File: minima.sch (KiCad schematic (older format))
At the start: 13 parts, among them J101 left_output, J102 left_input, J103 right_output, J104 right_input, J105 aux_power, J106 mains_voltage, J107 transformer_secondary, J108 transformer_primary, J109 earth

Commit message: The board shall now support single channel only.
Signed-off-by: Nenad Radulovic <nenad.radulovic@seavus.com>
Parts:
- removed J102: left_input, Connector_PinHeader_2.54mm:PinHeader_1x04_P2.54mm_Vertical, symbol Conn_01x04
- removed J103: right_output, Connector_Phoenix_MC:PhoenixContact_MCV_1,5_2-G-3.5_1x02_P3.50mm_Vertical, symbol Screw_Terminal_01x02
- removed J104: right_input, Connector_PinHeader_2.54mm:PinHeader_1x04_P2.54mm_Vertical, symbol Conn_01x04
- removed J105: aux_power, Connector_Phoenix_MC:PhoenixContact_MCV_1,5_4-G-3.5_1x04_P3.50mm_Vertical, symbol Conn_01x04
- removed J106: mains_voltage, Connector_Phoenix_MC:PhoenixContact_MCV_1,5_2-G-3.81_1x02_P3.81mm_Vertical, symbol Screw_Terminal_01x02
- removed J107: transformer_secondary, Connector_Phoenix_MC:PhoenixContact_MCV_1,5_3-G-3.5_1x03_P3.50mm_Vertical, symbol Screw_Terminal_01x03
- removed J108: transformer_primary, Connector_Phoenix_MC:PhoenixContact_MCV_1,5_2-G-3.81_1x02_P3.81mm_Vertical, symbol Screw_Terminal_01x02
- removed J109: earth, Connector_Phoenix_MC:PhoenixContact_MCV_1,5_2-G-5.08_1x02_P5.08mm_Vertical, symbol Screw_Terminal_01x02
- removed MH1, MH2: Mounting hole, MountingHole:MountingHole_3.2mm_M3_ISO14580_Pad, symbol Conn_01x01
- removed MH3, MH4: Mounting Hole, MountingHole:MountingHole_3.2mm_M3_ISO14580_Pad, symbol Conn_01x01
- added J102: input, TerminalBlock_Phoenix:TerminalBlock_Phoenix_MPT-0,5-4-2.54_1x04_P2.54mm_Horizontal, symbol Screw_Terminal_01x04
- added J103: powersupply, Connector_Phoenix_MC:PhoenixContact_MCV_1,5_6-G-3.5_1x06_P3.50mm_Vertical, symbol Screw_Terminal_01x06
- added J104: ps_ctrl, Connector_IDC:IDC-Header_2x05_P2.54mm_Vertical, symbol Conn_02x05_Odd_Even
- added LOGO1: KiCad Logo, Symbol:KiCad-Logo2_12mm_SilkScreen, symbol Mounting_Hole
- added LOGO2: OSHW Logo, Symbol:OSHW-Logo2_14.6x12mm_SilkScreen, symbol Mounting_Hole
- added MK101, MK102, MK103, MK104: Mounting_Hole, MountingHole:MountingHole_3.2mm_M3_ISO7380, symbol Mounting_Hole
- J101: value left_output -> output
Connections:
- net labels removed: GNDPWR, VDDA, VSSA
- wire segments 47 -> 57
- no-connect marks 4 -> 1
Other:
- note added: "ps_ctrl_gnd"
- note added: "ps_ctrl_i_reserved"
- note added: "ps_ctrl_o_reserved"
- note added: "ps_ctrl_op"
- note added: "ps_ctrl_outp"
- note added: "ps_ctrl_ovrld"
- note added: "ps_ctrl_vdd12"
- moved on the sheet: J101

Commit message: Switched to Kicad 5.0
Signed-off-by: Nenad Radulovic <nenad.b.radulovic@gmail.com>
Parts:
- removed J104: ps_ctrl, Connector_IDC:IDC-Header_2x05_P2.54mm_Vertical, symbol Conn_02x05_Odd_Even
- J1: renamed from J101; symbol Screw_Terminal_01x02 -> minima-rescue:Screw_Terminal_01x02
- J2: renamed from J102; symbol Screw_Terminal_01x04 -> minima-rescue:Screw_Terminal_01x04
- J3: renamed from J103; footprint Connector_Phoenix_MC:PhoenixContact_MCV_1,5_6-G-3.5_1x06_P3.50mm_Vertical -> Connector_Phoenix_MC:PhoenixContact_MCV_1,5_3-G-3.5_1x03_P3.50mm_Vertical; symbol Screw_Terminal_01x06 -> minima-rescue:Screw_Terminal_01x03
- LOGO1, LOGO2: symbol Mounting_Hole -> minima-rescue:Mounting_Hole
- MK1: renamed from MK101; symbol Mounting_Hole -> minima-rescue:Mounting_Hole
- MK2: renamed from MK102; symbol Mounting_Hole -> minima-rescue:Mounting_Hole
- MK3: renamed from MK103; symbol Mounting_Hole -> minima-rescue:Mounting_Hole
- MK4: renamed from MK104; symbol Mounting_Hole -> minima-rescue:Mounting_Hole
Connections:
- net labels added: GNDPWR
- wire segments 57 -> 18
- no-connect marks 1 -> 0
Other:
- note removed: "ps_ctrl_gnd"
- note removed: "ps_ctrl_i_reserved"
- note removed: "ps_ctrl_o_reserved"
- note removed: "ps_ctrl_op"
- note removed: "ps_ctrl_outp"
- note removed: "ps_ctrl_ovrld"
- note removed: "ps_ctrl_vdd12"
- moved on the sheet: J2

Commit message: Updated regarding v5.0
Still updateing regarding transition to v5.0
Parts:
- removed LOGO1: KiCad Logo, Symbol:KiCad-Logo2_12mm_SilkScreen, symbol minima-rescue:Mounting_Hole
- J1: symbol minima-rescue:Screw_Terminal_01x02 -> Connector:Screw_Terminal_01x02
- J2: symbol minima-rescue:Screw_Terminal_01x04 -> Connector:Screw_Terminal_01x04
- J3: symbol minima-rescue:Screw_Terminal_01x03 -> Connector:Screw_Terminal_01x03
- LOGO2: symbol minima-rescue:Mounting_Hole -> Graphic:Logo_Open_Hardware_Small
- MK1, MK2, MK3, MK4: symbol minima-rescue:Mounting_Hole -> Mechanical:MountingHole
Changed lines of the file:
@@
 $EndSheet
 $Comp
-L minima-rescue:Screw_Terminal_01x02 J1
+L Connector:Screw_Terminal_01x02 J1
 U 1 1 5ABB2BD1
 P 9100 1800
@@
 Connection ~ 2800 2100
 $Comp
-L minima-rescue:Mounting_Hole MK1
+L Mechanical:MountingHole MK1
 U 1 1 5AE4F4CA
 P 1200 6900
@@
 $EndComp
 $Comp
-L minima-rescue:Mounting_Hole MK3
+L Mechanical:MountingHole MK3
 U 1 1 5AE4FF11
 P 1200 7200
@@
 $EndComp
 $Comp
-L minima-rescue:Mounting_Hole MK4
+L Mechanical:MountingHole MK4
 U 1 1 5AE4FFFC
 P 2200 7200
@@
 $EndComp
 $Comp
-L minima-rescue:Mounting_Hole MK2
+L Mechanical:MountingHole MK2
 U 1 1 5AE500F0
 P 2200 6900
@@
 $EndComp
 $Comp
-L minima-rescue:Screw_Terminal_01x04 J2
+L Connector:Screw_Terminal_01x04 J2
 U 1 1 5AE50566
 P 2500 1900
@@
 $EndComp
 $Comp
-L minima-rescue:Screw_Terminal_01x03 J3
+L Connector:Screw_Terminal_01x03 J3
 U 1 1 5AE51422
 P 5550 4300
@@
 	5750 4200 6400 4200
 $Comp
-L minima-rescue:Mounting_Hole LOGO1
-U 1 1 5AE5636C
-P 2950 6900
-F 0 "LOGO1" H 2950 7100 50  0000 C CNN
-F 1 "KiCad Logo" H 2950 7025 50  0000 C CNN
-F 2 "Symbol:KiCad-Logo2_12mm_SilkScreen" H 2950 6900 50  0001 C CNN
-F 3 "" H 2950 6900 50  0001 C CNN
-	1    2950 6900
-	1    0    0    -1
-$EndComp
-$Comp
-L minima-rescue:Mounting_Hole LOGO2
+L Graphic:Logo_Open_Hardware_Small LOGO2
 U 1 1 5AE56655
 P 2950 7200

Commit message: Version 1.0b
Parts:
- added LOGO2: Kicad_Logo, Symbol:KiCad-Logo_5mm_Copper, symbol Graphic:Logo_Open_Hardware_Small
- J1: renamed from J2; footprint TerminalBlock_Phoenix:TerminalBlock_Phoenix_MPT-0,5-4-2.54_1x04_P2.54mm_Horizontal -> TerminalBlock_Phoenix:TerminalBlock_Phoenix_PT-1,5-3-3.5-H_1x03_P3.50mm_Horizontal; symbol Connector:Screw_Terminal_01x04 -> Connector_Generic:Conn_01x03
- J2: renamed from J3; footprint Connector_Phoenix_MC:PhoenixContact_MCV_1,5_3-G-3.5_1x03_P3.50mm_Vertical -> TerminalBlock_Phoenix:TerminalBlock_Phoenix_MKDS-3-3-5.08_1x03_P5.08mm_Horizontal
- J3: renamed from J1; footprint Connector_Phoenix_MC:PhoenixContact_MCV_1,5_2-G-3.5_1x02_P3.50mm_Vertical -> TerminalBlock_Phoenix:TerminalBlock_Phoenix_MKDS-3-2-5.08_1x02_P5.08mm_Horizontal
- LOGO1: renamed from LOGO2; footprint Symbol:OSHW-Logo2_14.6x12mm_SilkScreen -> Symbol:OSHW-Logo2_7.3x6mm_SilkScreen
- MK1, MK4: footprint MountingHole:MountingHole_3.2mm_M3_ISO7380 -> MountingHole:MountingHole_3.2mm_M3_ISO7380_Pad
- MK2: renamed from MK3; footprint MountingHole:MountingHole_3.2mm_M3_ISO7380 -> MountingHole:MountingHole_3.2mm_M3_ISO7380_Pad
- MK3: renamed from MK2; footprint MountingHole:MountingHole_3.2mm_M3_ISO7380 -> MountingHole:MountingHole_3.2mm_M3_ISO7380_Pad
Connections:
- wire segments 18 -> 16
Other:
- moved on the sheet: J3
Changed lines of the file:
@@
 F0 "Power supply" 60
 F1 "psupply.sch" 60
-F2 "ps_vcc" I L 6400 4200 60
-F3 "ps_vee" I L 6400 4300 60
-F4 "ps_gnd" I L 6400 4400 60
+F2 "ps_vcc" I L 6400 4400 60
+F3 "ps_vee" I L 6400 4200 60
+F4 "ps_gnd" I L 6400 4300 60
 $EndSheet
 $Comp
-L Connector:Screw_Terminal_01x02 J1
+L Connector:Screw_Terminal_01x02 J3
 U 1 1 5ABB2BD1
-P 9100 1800
-F 0 "J1" H 9100 1900 50  0000 C CNN
-F 1 "output" H 9100 1600 50  0000 C CNN
-F 2 "Connector_Phoenix_MC:PhoenixContact_MCV_1,5_2-G-3.5_1x02_P3.50mm_Vertical" H 9100 1800 50  0001 C CNN
-F 3 "http://www.farnell.com/datasheets/2138280.pdf" H 9100 1800 50  0001 C CNN
-F 4 "Farnell:3704816" H 9100 1800 60  0001 C CNN "Vendor"
-F 5 "Phoenix:1843606" H 9100 1800 60  0001 C CNN "Manufacturer"
-	1    9100 1800
+P 9100 1700
+F 0 "J3" H 9100 1800 50  0000 C CNN
+F 1 "output" H 9100 1500 50  0000 C CNN
+F 2 "TerminalBlock_Phoenix:TerminalBlock_Phoenix_MKDS-3-2-5.08_1x02_P5.08mm_Horizontal" H 9100 1700 50  0001 C CNN
+F 3 "http://www.farnell.com/datasheets/2138280.pdf" H 9100 1700 50  0001 C CNN
+F 4 "Farnell:3704816" H 9100 1700 60  0001 C CNN "Vendor"
+F 5 "Phoenix:1843606" H 9100 1700 60  0001 C CNN "Manufacturer"
+	1    9100 1700
 	1    0    0    -1
 $EndComp
@@
 Wire Wire Line
 	8000 1800 8900 1800
-Wire Wire Line
-	2700 2100 2800 2100
 Wire Notes Line
 	800  6600 2600 6600
@@
 Text Notes 800  6550 0    60   ~ 0
 Mounting components
-Connection ~ 2800 2100
 $Comp
 L Mechanical:MountingHole MK1
@@
 F 0 "MK1" H 1200 7100 50  0000 C CNN
 F 1 "Mounting_Hole" H 1200 7025 50  0000 C CNN
-F 2 "MountingHole:MountingHole_3.2mm_M3_ISO7380" H 1200 6900 50  0001 C CNN
+F 2 "MountingHole:MountingHole_3.2mm_M3_ISO7380_Pad" H 1200 6900 50  0001 C CNN
 F 3 "" H 1200 6900 50  0001 C CNN
 	1    1200 6900
@@
 $EndComp
 $Comp
-L Mechanical:MountingHole MK3
+L Mechanical:MountingHole MK2
 U 1 1 5AE4FF11
 P 1200 7200
-F 0 "MK3" H 1200 7400 50  0000 C CNN
+F 0 "MK2" H 1200 7400 50  0000 C CNN
 F 1 "Mounting_Hole" H 1200 7325 50  0000 C CNN
-F 2 "MountingHole:MountingHole_3.2mm_M3_ISO7380" H 1200 7200 50  0001 C CNN
+F 2 "MountingHole:MountingHole_3.2mm_M3_ISO7380_Pad" H 1200 7200 50  0001 C CNN
 F 3 "" H 1200 7200 50  0001 C CNN
 	1    1200 7200
@@
 F 0 "MK4" H 2200 7400 50  0000 C CNN
 F 1 "Mounting_Hole" H 2200 7325 50  0000 C CNN
-F 2 "MountingHole:MountingHole_3.2mm_M3_ISO7380" H 2200 7200 50  0001 C CNN
+F 2 "MountingHole:MountingHole_3.2mm_M3_ISO7380_Pad" H 2200 7200 50  0001 C CNN
 F 3 "" H 2200 7200 50  0001 C CNN
 	1    2200 7200
@@
 $EndComp
 $Comp
-L Mechanical:MountingHole MK2
+L Mechanical:MountingHole MK3
 U 1 1 5AE500F0
 P 2200 6900
-F 0 "MK2" H 2200 7100 50  0000 C CNN
+F 0 "MK3" H 2200 7100 50  0000 C CNN
 F 1 "Mounting_Hole" H 2200 7025 50  0000 C CNN
-F 2 "MountingHole:MountingHole_3.2mm_M3_ISO7380" H 2200 6900 50  0001 C CNN
+F 2 "MountingHole:MountingHole_3.2mm_M3_ISO7380_Pad" H 2200 6900 50  0001 C CNN
 F 3 "" H 2200 6900 50  0001 C CNN
 	1    2200 6900
@@
 $EndComp
 $Comp
-L Connector:Screw_Terminal_01x04 J2
+L Connector_Generic:Conn_01x03 J1
 U 1 1 5AE50566
 P 2500 1900
-F 0 "J2" H 2500 2100 50  0000 C CNN
+F 0 "J1" H 2500 2100 50  0000 C CNN
 F 1 "input" H 2500 1600 50  0000 C CNN
-F 2 "TerminalBlock_Phoenix:TerminalBlock_Phoenix_MPT-0,5-4-2.54_1x04_P2.54mm_Horizontal" H 2500 1900 50  0001 C CNN
+F 2 "TerminalBlock_Phoenix:TerminalBlock_Phoenix_PT-1,5-3-3.5-H_1x03_P3.50mm_Horizontal" H 2500 1900 50  0001 C CNN
 F 3 "" H 2500 1900 50  0001 C CNN
 	1    2500 1900
@@
 $EndComp
 $Comp
-L Connector:Screw_Terminal_01x03 J3
+L Connector:Screw_Terminal_01x03 J2
 U 1 1 5AE51422
 P 5550 4300
-F 0 "J3" H 5550 4600 50  0000 C CNN
+F 0 "J2" H 5550 4600 50  0000 C CNN
 F 1 "powersupply" H 5550 3900 50  0000 C CNN
-F 2 "Connector_Phoenix_MC:PhoenixContact_MCV_1,5_3-G-3.5_1x03_P3.50mm_Vertical" H 5550 4300 50  0001 C CNN
+F 2 "TerminalBlock_Phoenix:TerminalBlock_Phoenix_MKDS-3-3-5.08_1x03_P5.08mm_Horizontal" H 5550 4300 50  0001 C CNN
 F 3 "" H 5550 4300 50  0001 C CNN
 	1    5550 4300
@@
 	5750 4200 6400 4200
 $Comp
-L Graphic:Logo_Open_Hardware_Small LOGO2
+L Graphic:Logo_Open_Hardware_Small LOGO1
 U 1 1 5AE56655
 P 2950 7200
-F 0 "LOGO2" H 2950 7400 50  0000 C CNN
-F 1 "OSHW Logo" H 2950 7325 50  0000 C CNN
-F 2 "Symbol:OSHW-Logo2_14.6x12mm_SilkScreen" H 2950 7200 50  0001 C CNN
+F 0 "LOGO1" H 3200 7400 50  0000 L CNN
+F 1 "OSHW Logo" H 3200 7300 50  0000 L CNN
+F 2 "Symbol:OSHW-Logo2_7.3x6mm_SilkScreen" H 2950 7200 50  0001 C CNN
 F 3 "" H 2950 7200 50  0001 C CNN
 	1    2950 7200
 	1    0    0    -1
 $EndComp
-Wire Wire Line
-	2800 1900 2800 2100
-Wire Wire Line
-	2800 2100 2800 3200
-Wire Wire Line
-	2800 1900 2700 1900
 $Sheet
 S 3300 1600 1600 1300
@@
 Wire Wire Line
 	4900 1800 6400 1800
+Wire Wire Line
+	3000 3200 3000 2000
+Wire Wire Line
+	3000 2000 3300 2000
+Wire Wire Line
+	6100 3200 6100 2200
+Wire Wire Line
+	6100 2200 6400 2200
+Wire Wire Line
+	3000 3200 6100 3200
 $Comp
 L power:GNDPWR #PWR02
+U 1 1 5B625C49
+P 8800 2000
+F 0 "#PWR02" H 8800 1800 50  0001 C CNN
+F 1 "GNDPWR" H 8804 1846 50  0000 C CNN
+F 2 "" H 8800 1950 50  0001 C CNN
+F 3 "" H 8800 1950 50  0001 C CNN
+	1    8800 2000
+	1    0    0    -1
+$EndComp
+Connection ~ 3000 2000
+Wire Wire Line
+	3000 2000 2700 2000
+Wire Wire Line
+	2800 1900 2700 1900
+Wire Wire Line
+	2800 1900 2800 3200
+$Comp
+L power:GNDPWR #PWR01
 U 1 1 5B618FF8
 P 2800 3200
-F 0 "#PWR02" H 2800 3000 50  0001 C CNN
+F 0 "#PWR01" H 2800 3000 50  0001 C CNN
 F 1 "GNDPWR" H 2804 3046 50  0000 C CNN
 F 2 "" H 2800 3150 50  0001 C CNN
@@
 $EndComp
 Wire Wire Line
-	3000 3200 3000 2000
+	8800 1700 8900 1700
 Wire Wire Line
-	3000 2000 2700 2000
-Wire Wire Line
-	3000 2000 3300 2000
-Connection ~ 3000 2000
-Wire Wire Line
-	6100 3200 6100 2200
-Wire Wire Line
-	6100 2200 6400 2200
-Wire Wire Line
-	3000 3200 6100 3200
+	8800 1700 8800 2000
 $Comp
-L power:GNDPWR #PWR01
-U 1 1 5B625C49
-P 8800 2000
-F 0 "#PWR01" H 8800 1800 50  0001 C CNN
-F 1 "GNDPWR" H 8804 1846 50  0000 C CNN
-F 2 "" H 8800 1950 50  0001 C CNN
-F 3 "" H 8800 1950 50  0001 C CNN
-	1    8800 2000
+L Graphic:Logo_Open_Hardware_Small LOGO2
+U 1 1 5B612B64
+P 2950 6700
+F 0 "LOGO2" H 3197 6771 50  0000 L CNN
+F 1 "Kicad_Logo" H 3197 6680 50  0000 L CNN
+F 2 "Symbol:KiCad-Logo_5mm_Copper" H 2950 6700 50  0001 C CNN
+F 3 "~" H 2950 6700 50  0001 C CNN
+	1    2950 6700
 	1    0    0    -1
 $EndComp
-Wire Wire Line
-	8800 2000 8800 1900
-Wire Wire Line
-	8800 1900 8900 1900
 $EndSCHEMATC

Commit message: Release Version 1.0
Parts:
- J1: Manufacturer (none) -> Phoenix:MKDS1/3-3,5; Vendor (none) -> Farnell:2478587
- J2: Manufacturer (none) -> Phoenix:MKDSN2,5/3-5.08; Vendor (none) -> Farnell:1792767
- J3: Manufacturer Phoenix:1843606 -> Phoenix:MKDSN2,5/2-5.08; Vendor Farnell:3704816 -> Farnell:1792766
- renumbered LOGO2 to LOGO1, LOGO1 to LOGO2
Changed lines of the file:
@@
 F 1 "output" H 9100 1500 50  0000 C CNN
 F 2 "TerminalBlock_Phoenix:TerminalBlock_Phoenix_MKDS-3-2-5.08_1x02_P5.08mm_Horizontal" H 9100 1700 50  0001 C CNN
-F 3 "http://www.farnell.com/datasheets/2138280.pdf" H 9100 1700 50  0001 C CNN
-F 4 "Farnell:3704816" H 9100 1700 60  0001 C CNN "Vendor"
-F 5 "Phoenix:1843606" H 9100 1700 60  0001 C CNN "Manufacturer"
+F 3 "http://www.farnell.com/datasheets/2325421.pdf" H 9100 1700 50  0001 C CNN
+F 4 "Farnell:1792766" H 9100 1700 60  0001 C CNN "Vendor"
+F 5 "Phoenix:MKDSN2,5/2-5.08" H 9100 1700 60  0001 C CNN "Manufacturer"
 	1    9100 1700
 	1    0    0    -1
@@
 F 1 "input" H 2500 1600 50  0000 C CNN
 F 2 "TerminalBlock_Phoenix:TerminalBlock_Phoenix_PT-1,5-3-3.5-H_1x03_P3.50mm_Horizontal" H 2500 1900 50  0001 C CNN
-F 3 "" H 2500 1900 50  0001 C CNN
+F 3 "http://www.farnell.com/datasheets/2322648.pdf" H 2500 1900 50  0001 C CNN
+F 4 "Phoenix:MKDS1/3-3,5" H 0   0   50  0001 C CNN "Manufacturer"
+F 5 "Farnell:2478587" H 0   0   50  0001 C CNN "Vendor"
 	1    2500 1900
 	-1   0    0    -1
@@
 F 1 "powersupply" H 5550 3900 50  0000 C CNN
 F 2 "TerminalBlock_Phoenix:TerminalBlock_Phoenix_MKDS-3-3-5.08_1x03_P5.08mm_Horizontal" H 5550 4300 50  0001 C CNN
-F 3 "" H 5550 4300 50  0001 C CNN
+F 3 "http://www.farnell.com/datasheets/2325422.pdf" H 5550 4300 50  0001 C CNN
+F 4 "Phoenix:MKDSN2,5/3-5.08" H 0   0   50  0001 C CNN "Manufacturer"
+F 5 "Farnell:1792767" H 0   0   50  0001 C CNN "Vendor"
 	1    5550 4300
 	-1   0    0    -1
@@
 	5750 4200 6400 4200
 $Comp
-L Graphic:Logo_Open_Hardware_Small LOGO1
+L Graphic:Logo_Open_Hardware_Small LOGO2
 U 1 1 5AE56655
 P 2950 7200
-F 0 "LOGO1" H 3200 7400 50  0000 L CNN
+F 0 "LOGO2" H 3200 7400 50  0000 L CNN
 F 1 "OSHW Logo" H 3200 7300 50  0000 L CNN
 F 2 "Symbol:OSHW-Logo2_7.3x6mm_SilkScreen" H 2950 7200 50  0001 C CNN
@@
 	8800 1700 8800 2000
 $Comp
-L Graphic:Logo_Open_Hardware_Small LOGO2
+L Graphic:Logo_Open_Hardware_Small LOGO1
 U 1 1 5B612B64
 P 2950 6700
-F 0 "LOGO2" H 3197 6771 50  0000 L CNN
+F 0 "LOGO1" H 3197 6771 50  0000 L CNN
 F 1 "Kicad_Logo" H 3197 6680 50  0000 L CNN
 F 2 "Symbol:KiCad-Logo_5mm_Copper" H 2950 6700 50  0001 C CNN
@@
 	1    0    0    -1
 $EndComp
+$Comp
+L Graphic:Logo_Open_Hardware_Small #LOGO1
+U 1 1 5B6132D1
+P 4000 6700
+F 0 "#LOGO1" H 4000 6975 50  0001 C CNN
+F 1 "Logo_Open_Hardware_Small" H 4000 6475 50  0001 C CNN
+F 2 "" H 4000 6700 50  0001 C CNN
+F 3 "~" H 4000 6700 50  0001 C CNN
+	1    4000 6700
+	1    0    0    -1
+$EndComp

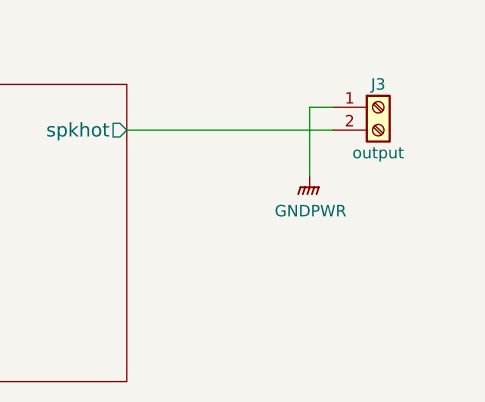
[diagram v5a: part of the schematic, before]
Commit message: Releasing version with distant psu caps.
Signed-off-by: Nenad Radulovic <nenad.b.radulovic@gmail.com>
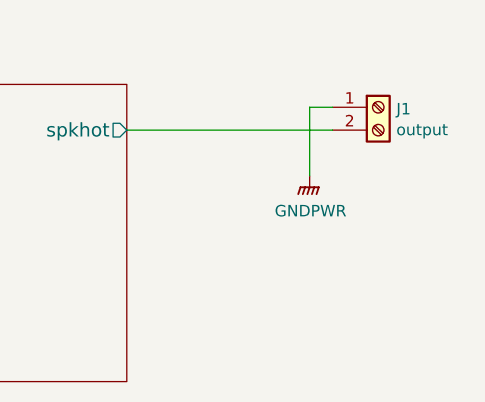
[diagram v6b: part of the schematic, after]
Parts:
- renumbered J3 to J1, J1 to J2, J2 to J3, MK3 to MK2, MK2 to MK3
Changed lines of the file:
@@
 $EndSheet
 $Comp
-L Connector:Screw_Terminal_01x02 J3
+L Connector:Screw_Terminal_01x02 J1
 U 1 1 5ABB2BD1
 P 9100 1700
-F 0 "J3" H 9100 1800 50  0000 C CNN
-F 1 "output" H 9100 1500 50  0000 C CNN
+F 0 "J1" H 9179 1692 50  0000 L CNN
+F 1 "output" H 9179 1601 50  0000 L CNN
 F 2 "TerminalBlock_Phoenix:TerminalBlock_Phoenix_MKDS-3-2-5.08_1x02_P5.08mm_Horizontal" H 9100 1700 50  0001 C CNN
 F 3 "http://www.farnell.com/datasheets/2325421.pdf" H 9100 1700 50  0001 C CNN
@@
 $EndComp
 $Comp
-L Mechanical:MountingHole MK2
+L Mechanical:MountingHole MK3
 U 1 1 5AE4FF11
 P 1200 7200
-F 0 "MK2" H 1200 7400 50  0000 C CNN
+F 0 "MK3" H 1200 7400 50  0000 C CNN
 F 1 "Mounting_Hole" H 1200 7325 50  0000 C CNN
 F 2 "MountingHole:MountingHole_3.2mm_M3_ISO7380_Pad" H 1200 7200 50  0001 C CNN
@@
 $EndComp
 $Comp
-L Mechanical:MountingHole MK3
+L Mechanical:MountingHole MK2
 U 1 1 5AE500F0
 P 2200 6900
-F 0 "MK3" H 2200 7100 50  0000 C CNN
+F 0 "MK2" H 2200 7100 50  0000 C CNN
 F 1 "Mounting_Hole" H 2200 7025 50  0000 C CNN
 F 2 "MountingHole:MountingHole_3.2mm_M3_ISO7380_Pad" H 2200 6900 50  0001 C CNN
@@
 $EndComp
 $Comp
-L Connector_Generic:Conn_01x03 J1
+L Connector_Generic:Conn_01x03 J2
 U 1 1 5AE50566
 P 2500 1900
-F 0 "J1" H 2500 2100 50  0000 C CNN
-F 1 "input" H 2500 1600 50  0000 C CNN
+F 0 "J2" H 2420 2217 50  0000 C CNN
+F 1 "input" H 2420 2126 50  0000 C CNN
 F 2 "TerminalBlock_Phoenix:TerminalBlock_Phoenix_PT-1,5-3-3.5-H_1x03_P3.50mm_Horizontal" H 2500 1900 50  0001 C CNN
 F 3 "http://www.farnell.com/datasheets/2322648.pdf" H 2500 1900 50  0001 C CNN
@@
 $EndComp
 $Comp
-L Connector:Screw_Terminal_01x03 J2
+L Connector:Screw_Terminal_01x03 J3
 U 1 1 5AE51422
 P 5550 4300
-F 0 "J2" H 5550 4600 50  0000 C CNN
-F 1 "powersupply" H 5550 3900 50  0000 C CNN
+F 0 "J3" H 5470 4617 50  0000 C CNN
+F 1 "powersupply" H 5470 4526 50  0000 C CNN
 F 2 "TerminalBlock_Phoenix:TerminalBlock_Phoenix_MKDS-3-3-5.08_1x03_P5.08mm_Horizontal" H 5550 4300 50  0001 C CNN
 F 3 "http://www.farnell.com/datasheets/2325422.pdf" H 5550 4300 50  0001 C CNN
@@
 	3000 3200 6100 3200
 $Comp
-L power:GNDPWR #PWR02
+L power:GNDPWR #PWR01
 U 1 1 5B625C49
 P 8800 2000
-F 0 "#PWR02" H 8800 1800 50  0001 C CNN
+F 0 "#PWR01" H 8800 1800 50  0001 C CNN
 F 1 "GNDPWR" H 8804 1846 50  0000 C CNN
 F 2 "" H 8800 1950 50  0001 C CNN
@@
 	2800 1900 2800 3200
 $Comp
-L power:GNDPWR #PWR01
+L power:GNDPWR #PWR02
 U 1 1 5B618FF8
 P 2800 3200
-F 0 "#PWR01" H 2800 3000 50  0001 C CNN
+F 0 "#PWR02" H 2800 3000 50  0001 C CNN
 F 1 "GNDPWR" H 2804 3046 50  0000 C CNN
 F 2 "" H 2800 3150 50  0001 C CNN

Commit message: Relase v1.0
Corrected a few things on the PCB.
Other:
- note added: "Return speaker ground at the\njunction of bypass capacitors \nnear power IC."
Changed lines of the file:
@@
 	1    0    0    -1
 $EndComp
-$Comp
-L Graphic:Logo_Open_Hardware_Small #LOGO1
-U 1 1 5B6132D1
-P 4000 6700
-F 0 "#LOGO1" H 4000 6975 50  0001 C CNN
-F 1 "Logo_Open_Hardware_Small" H 4000 6475 50  0001 C CNN
-F 2 "" H 4000 6700 50  0001 C CNN
-F 3 "~" H 4000 6700 50  0001 C CNN
-	1    4000 6700
-	1    0    0    -1
-$EndComp
+Text Notes 9100 2150 0    50   ~ 0
+Return speaker ground at the\njunction of bypass capacitors \nnear power IC.
 $EndSCHEMATC

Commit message: Release version v1.1
Signed-off-by: Nenad Radulovic <nenad.b.radulovic@gmail.com>
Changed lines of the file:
@@
 F2 "inp" I L 3300 1800 50
 F3 "outp" O R 4900 1800 50
-F4 "sgnd" I L 3300 2000 50
+F4 "sgnd" I L 3300 1900 50
 $EndSheet
 Wire Wire Line
 	4900 1800 6400 1800
 Wire Wire Line
-	3000 3200 3000 2000
+	3000 3200 3000 1900
 Wire Wire Line
-	3000 2000 3300 2000
+	3000 1900 3300 1900
 Wire Wire Line
 	6100 3200 6100 2200
@@
 	1    0    0    -1
 $EndComp
-Connection ~ 3000 2000
 Wire Wire Line
-	3000 2000 2700 2000
+	3000 1900 2700 1900
 Wire Wire Line
-	2800 1900 2700 1900
-Wire Wire Line
-	2800 1900 2800 3200
+	2800 2000 2800 3200
 $Comp
 L power:GNDPWR #PWR02
@@
 Text Notes 9100 2150 0    50   ~ 0
 Return speaker ground at the\njunction of bypass capacitors \nnear power IC.
+Wire Wire Line
+	2800 2000 2700 2000
+Connection ~ 3000 1900
 $EndSCHEMATC
